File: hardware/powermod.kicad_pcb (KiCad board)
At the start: 4 copper layers, 65 x 40 mm, 77 parts, among them J1 USB_C_IN, J2 USB_C_OUT, J3 JST_PH_2, J4 STEMMA_QT, J5 SWD_HDR, Q1 AON7407, Q2 AON7407, Q3 BSS138, SW1 BUTTON, U1 BM8563, U2 PY32F003F18P6, U3 TPS63020DSJR, U4 TP4056, U5 XC6206P332MR, Y1 32.768kHz

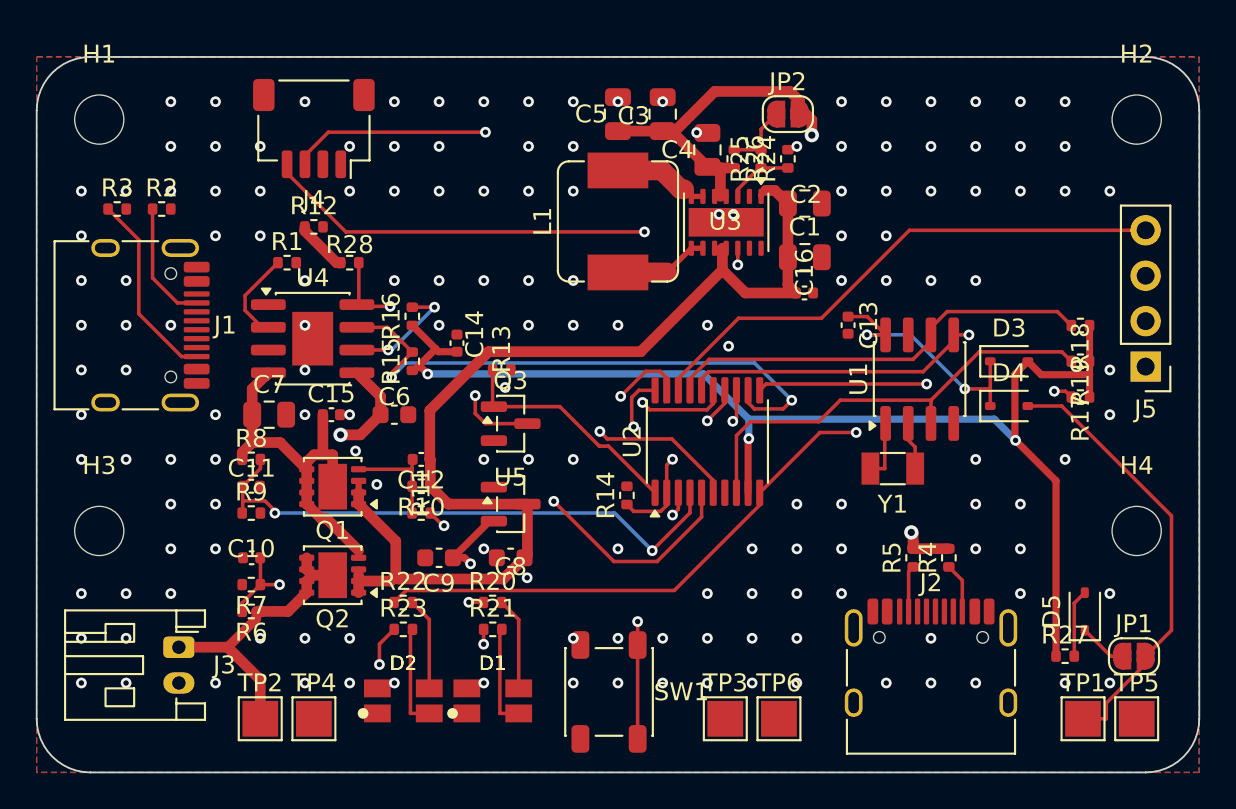
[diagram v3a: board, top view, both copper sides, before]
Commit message: hardware: final routed board - CC on A5/B5, 0 DRC, 0 unrouted
User completed routing. Full verification: DRC 0 violations, 0 unrouted,
pad-diff 226/226. USB-C CC correctly on A5/B5 (A8/B8 NC). L1N/L2 uniform 1.1mm.
U3 EP = 2 tented GND ties (max that fits; inner-layer routing fills the band;
EP sits over the In1 solid GND plane + pour). 431 tracks, 194 vias.

Co-Authored-By: Claude Opus 4.8 <noreply@anthropic.com>
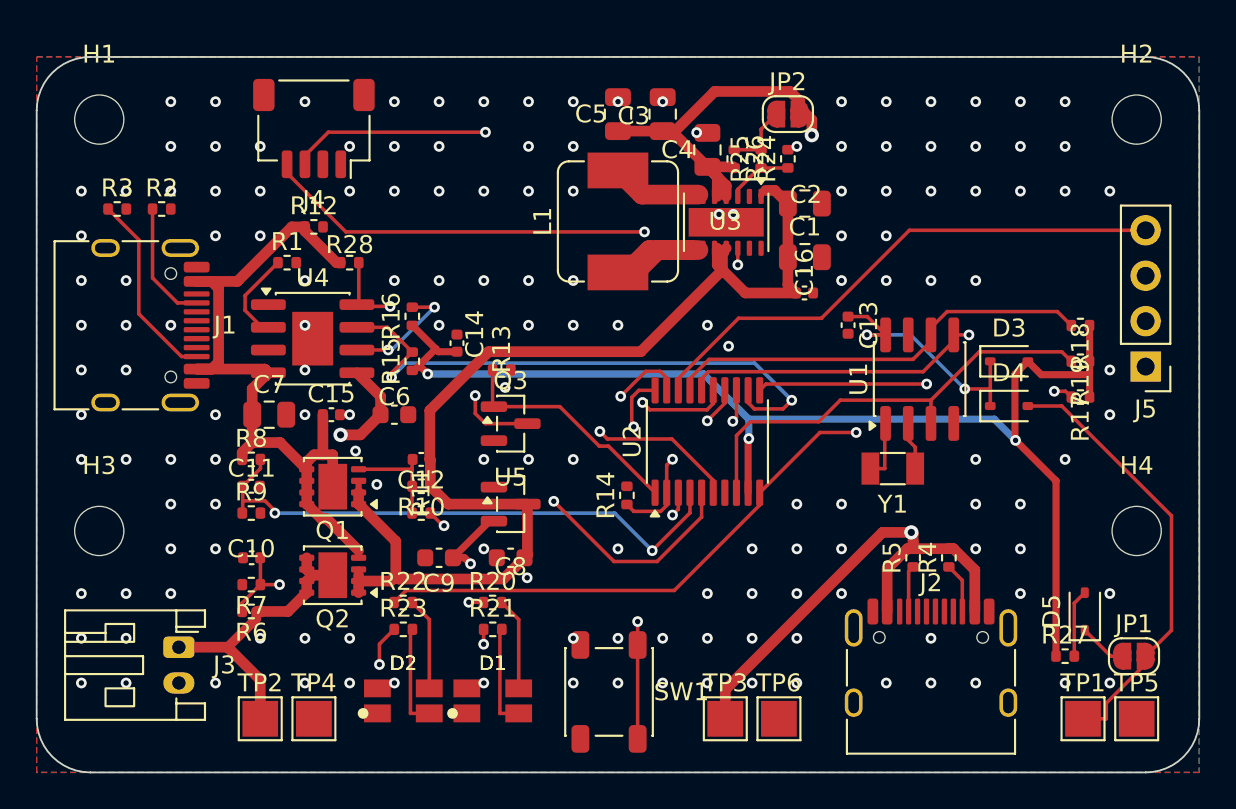
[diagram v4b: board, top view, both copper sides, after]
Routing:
- net VOUT: track 47.8 -> 73.8 mm
- net VBUS: track 24.5 -> 42.8 mm
- net L1N: track 5.31 -> 9.64 mm
- net VSYS: track 63.9 -> 64.7 mm
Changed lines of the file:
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@@
 	)
 	(segment
+		(start 10.17 17.065252)
+		(end 10.17 12.934748)
+		(width 0.6)
+		(layer "F.Cu")
+		(net "VBUS")
+	)
+	(segment
+		(start 9.785252 17.45)
+		(end 10.17 17.065252)
+		(width 0.6)
+		(layer "F.Cu")
+		(net "VBUS")
+	)
+	(segment
 		(start 12.05 18.56)
 		(end 12.05 20)
@@
 	)
 	(segment
+		(start 14.268232 9.5)
+		(end 14.99 9.5)
+		(width 0.6)
+		(layer "F.Cu")
+		(net "VBUS")
+	)
+	(segment
 		(start 13.6055 21.5555)
 		(end 12.05 21.5555)
@@
 	)
 	(segment
+		(start 8.945 17.45)
+		(end 12.75 17.45)
+		(width 0.6)
+		(layer "F.Cu")
+		(net "VBUS")
+	)
+	(segment
 		(start 16.99 11.5)
 		(end 16.7667 11.5)
@@
 	)
 	(segment
+		(start 11.218232 12.55)
+		(end 14.268232 9.5)
+		(width 0.6)
+		(layer "F.Cu")
+		(net "VBUS")
+	)
+	(segment
+		(start 10.17 12.934748)
+		(end 9.785252 12.55)
+		(width 0.6)
+		(layer "F.Cu")
+		(net "VBUS")
+	)
+	(segment
 		(start 15.1 23.05)
 		(end 15.1 22.6466)
@@
 	)
 	(segment
+		(start 8.945 12.55)
+		(end 11.218232 12.55)
+		(width 0.6)
+		(layer "F.Cu")
+		(net "VBUS")
+	)
+	(segment
 		(start 16.2215 25.8165)
 		(end 15.9165 25.8165)
@@
 	)
 	(segment
+		(start 8.945 17.45)
+		(end 9.785252 17.45)
+		(width 0.6)
+		(layer "F.Cu")
+		(net "VBUS")
+	)
+	(segment
+		(start 12.75 17.45)
+		(end 12.955 17.655)
+		(width 0.6)
+		(layer "F.Cu")
+		(net "VBUS")
+	)
+	(segment
 		(start 12.7728 17.8372)
 		(end 12.7667 17.8433)
@@
 	)
 	(segment
+		(start 9.785252 12.55)
+		(end 8.945 12.55)
+		(width 0.6)
+		(layer "F.Cu")
+		(net "VBUS")
+	)
+	(segment
 		(start 15.1 25)
 		(end 15.1 24.35)
@@
 	)
 	(segment
+		(start 38.3402 10.9048)
+		(end 38.55 10.695)
+		(width 0.6)
+		(layer "F.Cu")
+		(net "VSYS")
+	)
+	(segment
 		(start 23.01 25)
 		(end 27.4375 25)
@@
 	(segment
 		(start 38.3402 11.9107)
-		(end 39.6245 13.195)
+		(end 38.3402 10.9048)
 		(width 0.6)
 		(layer "F.Cu")
@@
 	)
 	(segment
-		(start 18 24.35)
-		(end 18 23.7)
-		(width 0.3504)
-		(layer "F.Cu")
-		(net "VSYS")
-	)
-	(segment
-		(start 38.3402 10.695)
-		(end 38.3998 10.695)
-		(width 0.3004)
+		(start 38.3402 11.9107)
+		(end 39.6245 13.195)
+		(width 0.6)
 		(layer "F.Cu")
 		(net "VSYS")
 	)
 	(segment
-		(start 38.3402 10.695)
-		(end 38.3402 11.9107)
-		(width 0.6)
+		(start 18 24.35)
+		(end 18 23.7)
+		(width 0.3504)
 		(layer "F.Cu")
 		(net "VSYS")
@@
 	)
 	(segment
-		(start 37.9 10.695)
-		(end 38.3402 10.695)
-		(width 0.3004)
+		(start 38.3402 11.9107)
+		(end 38.0498 11.6203)
+		(width 0.6)
 		(layer "F.Cu")
 		(net "VSYS")
@@
 	)
 	(segment
-		(start 38.4 10.695)
-		(end 38.55 10.695)
-		(width 0.3004)
-		(layer "F.Cu")
-		(net "VSYS")
-	)
-	(segment
 		(start 19.7933 29.3)
 		(end 20.0779 29.0154)
@@
 	)
 	(segment
+		(start 38.0498 11.6203)
+		(end 38.0498 10.695)
+		(width 0.6)
+		(layer "F.Cu")
+		(net "VSYS")
+	)
+	(segment
 		(start 20.0779 27.0779)
 		(end 20.0779 29.0154)
@@
 	)
 	(segment
-		(start 38.4 10.695)
-		(end 38.3998 10.695)
-		(width 0.6)
-		(layer "F.Cu")
-		(net "VSYS")
-	)
-	(segment
 		(start 20.99 23.05)
 		(end 20.99 24)
@@
 	)
 	(segment
-		(start 49 27.0849)
-		(end 49 26.6798)
+		(start 38.55 7.195)
+		(end 38.55 7.795)
 		(width 0.6)
 		(layer "F.Cu")
@@
 	)
 	(segment
-		(start 49 27.49)
-		(end 49 27.4884)
+		(start 49 27.0849)
+		(end 49 26.6798)
 		(width 0.6)
 		(layer "F.Cu")
@@
 	)
 	(segment
-		(start 38.55 7.795)
-		(end 38.225 7.795)
-		(width 0.3004)
+		(start 49 27.49)
+		(end 49 27.4884)
+		(width 0.6)
 		(layer "F.Cu")
 		(net "VOUT")
@@
 	)
 	(segment
-		(start 49 27.4868)
-		(end 49 27.4836)
+		(start 38.5 35.368629)
+		(end 47.288229 26.5804)
 		(width 0.6)
 		(layer "F.Cu")
@@
 	)
 	(segment
-		(start 38.225 6.205)
-		(end 37.56 6.205)
+		(start 51.258629 27.49)
+		(end 51 27.49)
+		(width 0.6)
+		(layer "F.Cu")
+		(net "VOUT")
+	)
+	(segment
+		(start 49 27.4868)
+		(end 49 27.4836)
 		(width 0.6)
 		(layer "F.Cu")
@@
 	)
 	(segment
+		(start 38.5 37)
+		(end 38.5 35.368629)
+		(width 0.6)
+		(layer "F.Cu")
+		(net "VOUT")
+	)
+	(segment
+		(start 37.5 6.145)
+		(end 38.0498 6.6948)
+		(width 0.6)
+		(layer "F.Cu")
+		(net "VOUT")
+	)
+	(segment
+		(start 47.288229 26.5804)
+		(end 48.9006 26.5804)
+		(width 0.6)
+		(layer "F.Cu")
+		(net "VOUT")
+	)
+	(segment
+		(start 52.45 28.681371)
+		(end 51.258629 27.49)
+		(width 0.6)
+		(layer "F.Cu")
+		(net "VOUT")
+	)
+	(segment
+		(start 48.680001 27.49)
+		(end 49 27.49)
+		(width 0.6)
+		(layer "F.Cu")
+		(net "VOUT")
+	)
+	(segment
 		(start 49 27.4873)
 		(end 49 27.4872)
@@
 	)
 	(segment
-		(start 39 6.205)
-		(end 38.225 6.205)
+		(start 52.45 31.005)
+		(end 52.45 28.681371)
 		(width 0.6)
 		(layer "F.Cu")
@@
 	)
 	(segment
-		(start 49 27.4884)
-		(end 49 27.4876)
+		(start 38.94 6.145)
+		(end 39 6.205)
 		(width 0.6)
 		(layer "F.Cu")
@@
 	)
 	(segment
-		(start 37.56 6.205)
-		(end 37.5 6.145)
+		(start 49 27.4884)
+		(end 49 27.4876)
 		(width 0.6)
 		(layer "F.Cu")
@@
 	)
 	(segment
-		(start 38.225 7.795)
-		(end 38.225 6.205)
+		(start 38.0498 6.6948)
+		(end 38.0498 7.795)
 		(width 0.6)
 		(layer "F.Cu")
@@
 	)
 	(segment
+		(start 37.5 6.145)
+		(end 38.55 7.195)
+		(width 0.6)
+		(layer "F.Cu")
+		(net "VOUT")
+	)
+	(segment
 		(start 49 27.4872)
 		(end 49 27.4868)
@@
 	)
 	(segment
+		(start 47.55 28.620001)
+		(end 48.680001 27.49)
+		(width 0.6)
+		(layer "F.Cu")
+		(net "VOUT")
+	)
+	(segment
 		(start 43.338 3.5153)
 		(end 43.338 4.3704)
@@
 	)
 	(segment
-		(start 38.225 7.795)
-		(end 37.9 7.795)
-		(width 0.3004)
+		(start 37.5 6.145)
+		(end 38.94 6.145)
+		(width 0.6)
 		(layer "F.Cu")
 		(net "VOUT")
@@
 	)
 	(segment
+		(start 47.55 31.005)
+		(end 47.55 28.620001)
+		(width 0.6)
+		(layer "F.Cu")
+		(net "VOUT")
+	)
+	(segment
 		(start 49 27.4836)
 		(end 49 27.4773)
@@
 	)
 	(segment
-		(start 36.2012 7.3962)
-		(end 36.6 7.795)
-		(width 0.3004)
+		(start 33.85 7.695)
+		(end 36.9998 7.695)
+		(width 1.1)
 		(layer "F.Cu")
 		(net "L2")
 	)
 	(segment
-		(start 34.9517 6.345)
-		(end 36.0029 7.3962)
+		(start 32.5 6.345)
+		(end 33.85 7.695)
 		(width 1.1)
 		(layer "F.Cu")
@@
 	)
 	(segment
-		(start 36.0029 7.3962)
-		(end 36.2012 7.3962)
+		(start 34.705 10.795)
+		(end 36.9998 10.795)
 		(width 1.1)
 		(layer "F.Cu")
-		(net "L2")
+		(net "L1N")
 	)
 	(segment
-		(start 37.25 7.795)
-		(end 36.6 7.795)
-		(width 0.3004)
+		(start 33.455 12.045)
+		(end 34.705 10.795)
+		(width 1.1)
 		(layer "F.Cu")
-		(net "L2")
+		(net "L1N")
 	)
 	(segment
-		(start 32.5 6.345)
-		(end 34.9517 6.345)
+		(start 34.25 10.795)
+		(end 36.6 10.795)
 		(width 1.1)
 		(layer "F.Cu")
-		(net "L2")
+		(net "L1N")
 	)
 	(segment
-		(start 35.25 12.045)
-		(end 36.6 10.695)
-		(width 0.3004)
+		(start 32.5 12.045)
+		(end 33 12.045)
+		(width 1.1)
 		(layer "F.Cu")
 		(net "L1N")
 	)
 	(segment
-		(start 36.6 10.695)
-		(end 37.25 10.695)
-		(width 0.3004)
+		(start 33 12.045)
+		(end 34.25 10.795)
+		(width 1.1)
 		(layer "F.Cu")
 		(net "L1N")
@@
 	(segment
 		(start 32.5 12.045)
-		(end 35.25 12.045)
+		(end 33.455 12.045)
 		(width 1.1)
 		(layer "F.Cu")

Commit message: hardware: full reroute after U2 -2.5mm move - EP now 4 GND ties
User moved U2 down 2.5mm to relieve the U3<->U2 signal corridor. Freerouting
then routed SCL/SDA/CONV_EN clear of the U3 EP, leaving the center band open.
Placed the full 2x2 tented GND tie grid = 4 EP ties (0 foreign).

Cleanest seed yet: CC on A5/B5, pad-diff 226/226, 0 shorts/clearance. Unrouted
= only the 4 USB-C power escapes (J1/J2 A4/A9); TP3 + the prior VOUT/CC
stragglers all routed. Remaining: 4 track_width (L1N/L2 necks) + the escapes.

Co-Authored-By: Claude Opus 4.8 <noreply@anthropic.com>
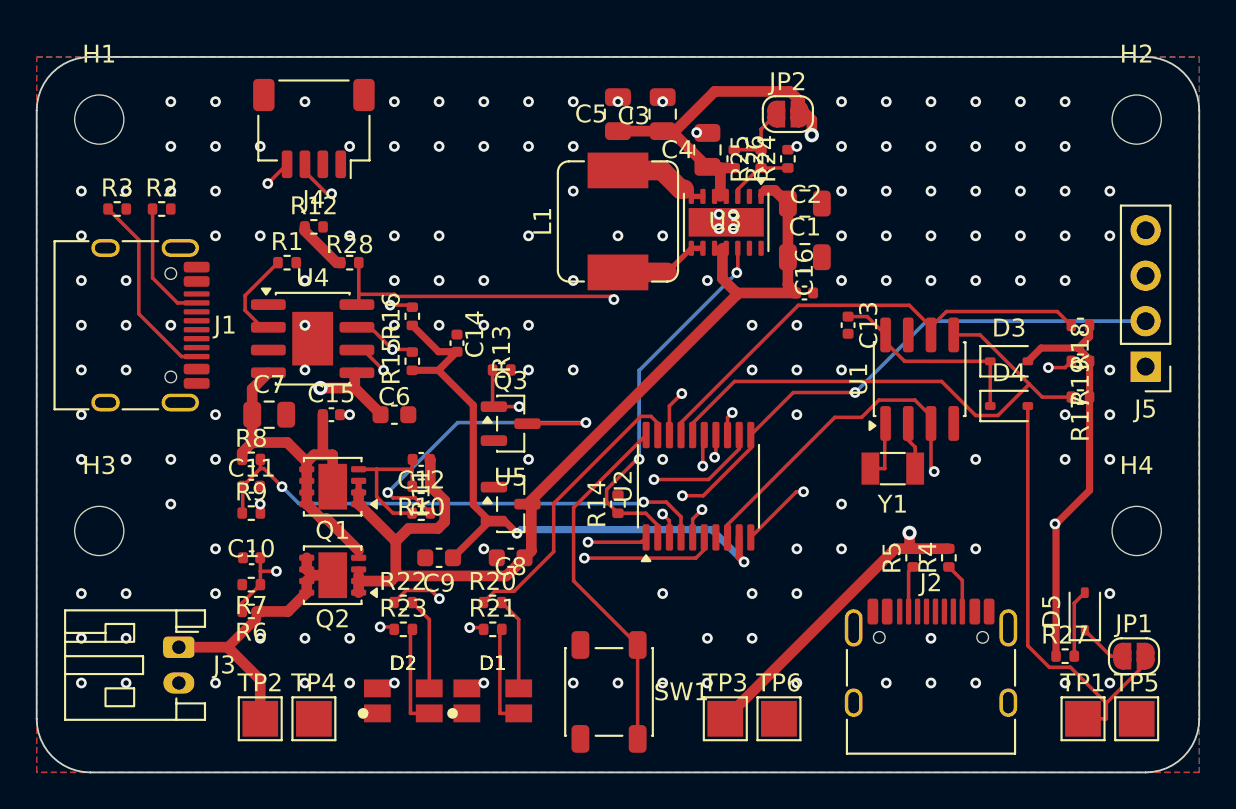
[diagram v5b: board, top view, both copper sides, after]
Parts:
- moved U2 2.55 mm to (37.0, 24.0)
- moved R14 0.70 mm to (32.5, 25.0)
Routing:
- net VBUS: track 42.8 -> 24.3 mm
- net LED_BAT_B: track 68.3 -> 51.6 mm, vias 2 -> 3
- net NRST: track 30.2 -> 42.2 mm, vias 0 -> 1
- net VOUT: track 73.8 -> 62.2 mm
- net LED_BAT_A: track 50.3 -> 60.8 mm, vias 1 -> 2
- net SDA: track 40.3 -> 31.2 mm
- net 3V3: track 85.7 -> 76.6 mm, vias 4 -> 3
- net VSYS: track 64.7 -> 58.2 mm
- net RTC_SDA: track 24.0 -> 30.0 mm, vias 2 -> 0
- net Q3_DRAIN: track 13.2 -> 18.9 mm
- net SCL: track 39.6 -> 34.5 mm
- net CHG_CHRG: track 32.6 -> 27.7 mm
- net L1N: track 9.64 -> 5.31 mm
- net VBAT_DIV: track 32.8 -> 28.7 mm
- net CHG_STDBY: track 26.9 -> 30.3 mm
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
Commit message: hardware: reroute after R14 move - pre-placed GND vias fix EP + R14.2
R14 moved to open space (35.5,29.5) but the autorouter still boxed its GND pad.
Solved both recurring issues deterministically by PRE-PLACING fixed GND vias on
the stripped board before DSN export, so Freerouting routes around them:
  - 4 EP tented GND ties (no seed-dependent signal crossing the band)
  - 1 R14.2 edge tie via (kills the floating GND island for good)

pad-diff 226/226, CC on A5/B5, 0 shorts/clearance, EP 4 ties, R14.2 tied.
Unrouted (this seed): 4 USB-C escapes + TP3 + R5.2 (VOUT). Plus 4 track_width
(L1N/L2 necks). 427 tracks.

Co-Authored-By: Claude Opus 4.8 <noreply@anthropic.com>
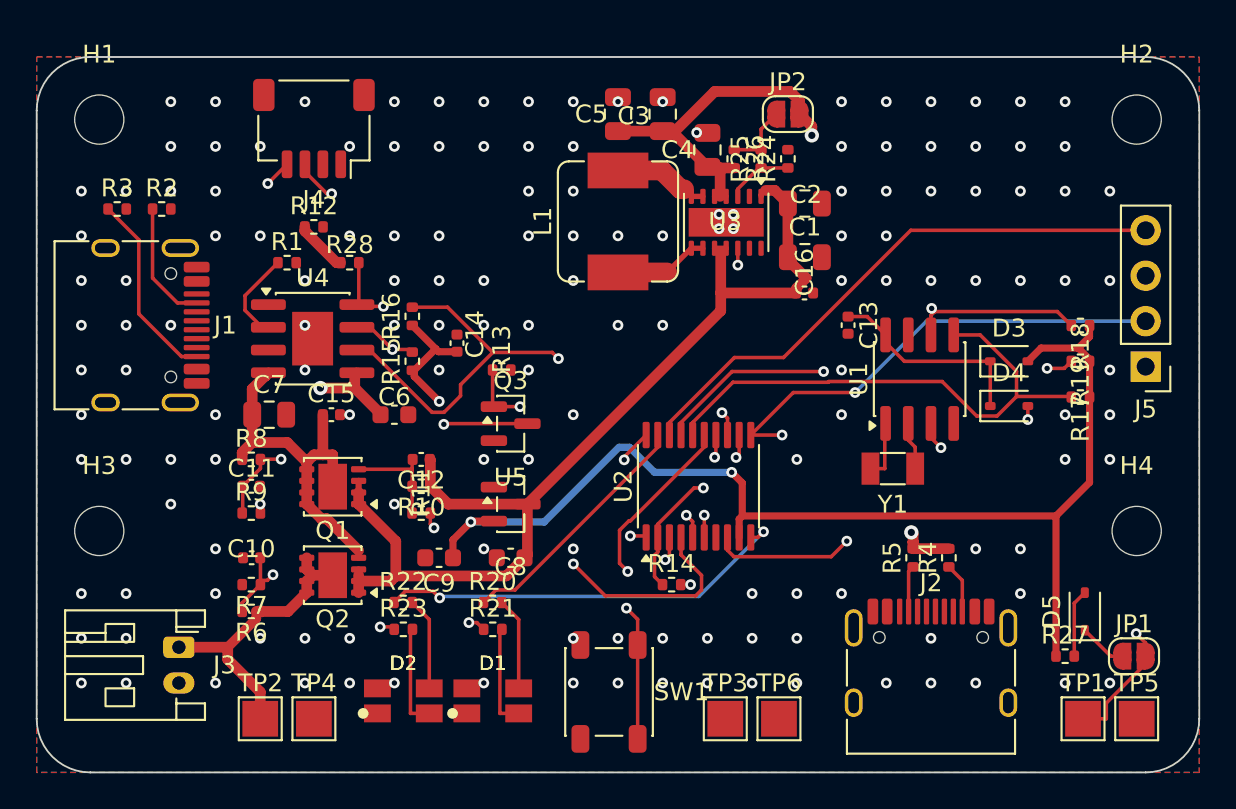
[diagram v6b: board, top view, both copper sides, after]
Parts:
- moved R14 5.41 mm to (35.5, 29.5), turned to 0 degrees
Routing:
- net VOUT: track 62.2 -> 47.6 mm
- net NRST: track 42.2 -> 31.8 mm, vias 1 -> 0
- net LED_BAT_A: track 60.8 -> 53.3 mm
- net Q3_DRAIN: track 18.9 -> 11.6 mm
- net VBUS_DIV: track 29.3 -> 34.8 mm
- net CHG_CE: track 33.4 -> 29.1 mm
- net LED_BAT_B: track 51.6 -> 55.6 mm
- net CHG_STDBY: track 30.3 -> 33.5 mm, vias 3 -> 2
- net 3V3: track 76.6 -> 79.7 mm
- net LED_PWR_A: track 16.5 -> 14.0 mm
- net VBACKUP: track 24.8 -> 22.4 mm, vias 0 -> 2
- net Q1_GATE: track 8.40 -> 6.00 mm
- net Q1_GATE_DRV: track 16.0 -> 14.2 mm
- net CONV_EN: track 21.4 -> 22.6 mm
- net VSYS: track 58.2 -> 59.1 mm
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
